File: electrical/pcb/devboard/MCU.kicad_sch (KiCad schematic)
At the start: 3 parts, among them U2 ESP32-S3-WROOM-1

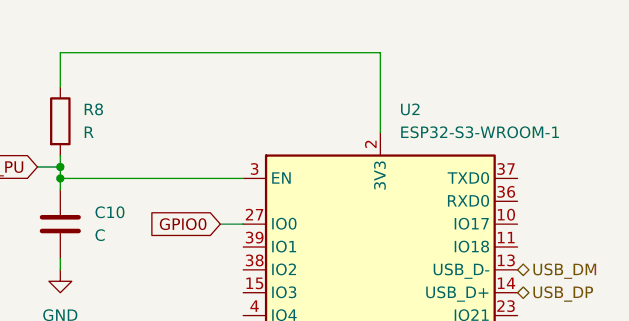
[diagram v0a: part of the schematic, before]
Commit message: cell shifter routed
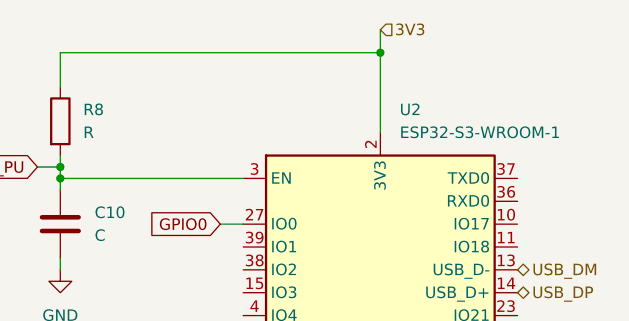
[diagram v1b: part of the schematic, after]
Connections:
- net 3V3: now reaches R8.1, U2.2 (3V3)
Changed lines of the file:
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@@
+		(color 0 0 0 0)
+	)
+	(junction
+		(at 140.97 53.34)
+		(diameter 0)
 		(color 0 0 0 0)
 	)
@@
 		(pts
 			(xy 140.97 62.23) (xy 140.97 53.34)
+		)
+		(stroke
+			(width 0)
+			(type default)
+		)
+	)
+	(wire
+		(pts
+			(xy 140.97 50.8) (xy 140.97 53.34)
 		)
 		(stroke
@@
 		)
 	)
+	(hierarchical_label "3V3"
+		(shape input)
+		(at 140.97 50.8 0)
+		(effects
+			(font
+				(size 1.27 1.27)
+			)
+			(justify left)
+		)
+	)

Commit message: Add files via upload
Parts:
- C10: footprint (none) -> Capacitor_SMD:C_0603_1608Metric
- R8: footprint (none) -> Resistor_SMD:R_0603_1608Metric
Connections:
- net SDA: now reaches U2.10 (IO17)
- net SCL: now reaches U2.11 (IO18)
- net OFF: now reaches U2.23 (IO21)
- net TEMP_VAL: now reaches U2.39 (IO1)
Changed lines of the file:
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@@
+	(wire
+		(pts
+			(xy 156.21 74.93) (xy 163.83 74.93)
+		)
+		(stroke
+			(width 0)
+			(type default)
+		)
+	)
 	(wire
 		(pts
@@
 		)
 	)
+	(global_label "OFF"
+		(shape input)
+		(at 156.21 82.55 0)
+		(fields_autoplaced yes)
+		(effects
+			(font
+				(size 1.27 1.27)
+			)
+			(justify left)
+		)
+		(property "Intersheetrefs" "${INTERSHEET_REFS}"
+			(at 162.7029 82.55 0)
+			(effects
+				(font
+					(size 1.27 1.27)
+				)
+				(justify left)
+				(hide yes)
+			)
+		)
+	)
+	(global_label "SDA"
+		(shape input)
+		(at 156.21 72.39 0)
+		(fields_autoplaced yes)
+		(effects
+			(font
+				(size 1.27 1.27)
+			)
+			(justify left)
+		)
+		(property "Intersheetrefs" "${INTERSHEET_REFS}"
+			(at 162.7633 72.39 0)
+			(effects
+				(font
+					(size 1.27 1.27)
+				)
+				(justify left)
+				(hide yes)
+			)
+		)
+	)
+	(global_label "SCL"
+		(shape input)
+		(at 163.83 74.93 0)
+		(fields_autoplaced yes)
+		(effects
+			(font
+				(size 1.27 1.27)
+			)
+			(justify left)
+		)
+		(property "Intersheetrefs" "${INTERSHEET_REFS}"
+			(at 170.3228 74.93 0)
+			(effects
+				(font
+					(size 1.27 1.27)
+				)
+				(justify left)
+				(hide yes)
+			)
+		)
+	)
 	(global_label "CHIP_PU"
 		(shape input)
@@
 		(property "Intersheetrefs" "${INTERSHEET_REFS}"
 			(at 91.8414 66.04 0)
+			(effects
+				(font
+					(size 1.27 1.27)
+				)
+				(justify right)
+				(hide yes)
+			)
+		)
+	)
+	(global_label "TEMP_VAL"
+		(shape input)
+		(at 125.73 74.93 180)
+		(fields_autoplaced yes)
+		(effects
+			(font
+				(size 1.27 1.27)
+			)
+			(justify right)
+		)
+		(property "Intersheetrefs" "${INTERSHEET_REFS}"
+			(at 113.7339 74.93 0)
 			(effects
 				(font
@@
 			)
 		)
-		(property "Footprint" ""
+		(property "Footprint" "Capacitor_SMD:C_0603_1608Metric"
 			(at 106.3752 76.2 0)
 			(effects
@@
 			)
 		)
-		(property "Footprint" ""
+		(property "Footprint" "Resistor_SMD:R_0603_1608Metric"
 			(at 103.632 60.96 90)
 			(effects
